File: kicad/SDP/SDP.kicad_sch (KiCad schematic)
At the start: 86 parts, among them J1 GPIO, J18 12V, J24 POWER, J25 Conn_01x04, J26 Conn_01x02, J27 MOTOR, J3 UART, J4 I2C, J5 Conn_01x04, J6 Conn_01x04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

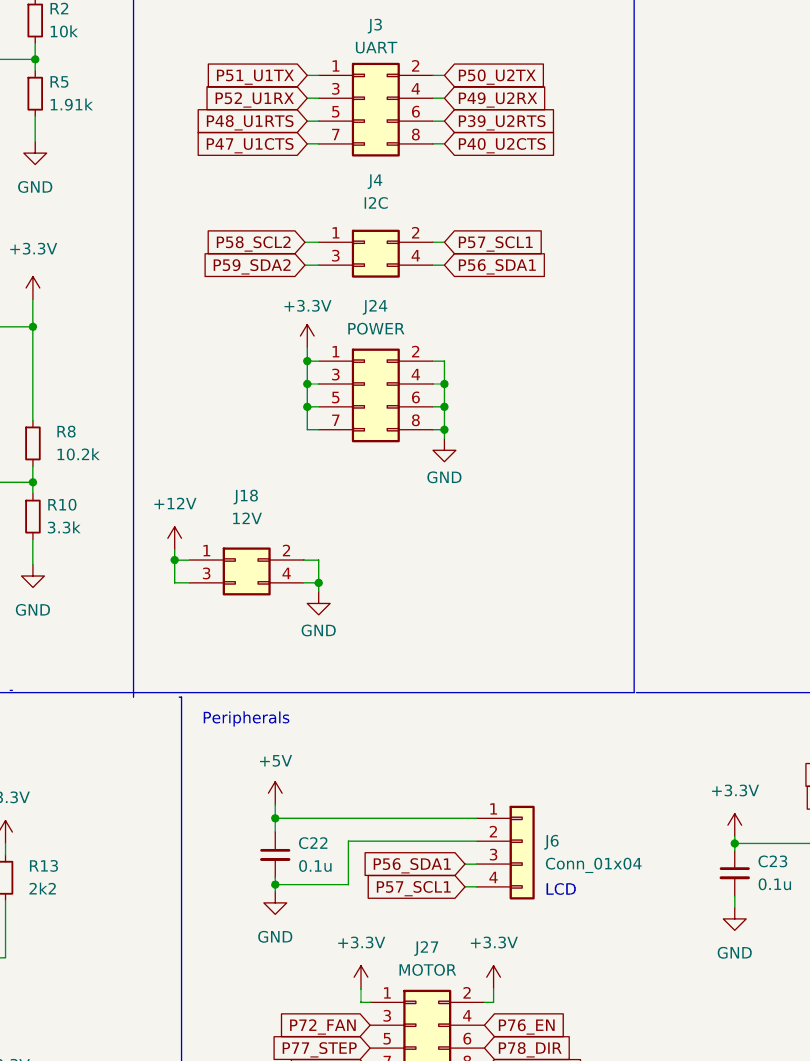
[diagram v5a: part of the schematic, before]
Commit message: Controller and motor PCB silkscreen and final layout
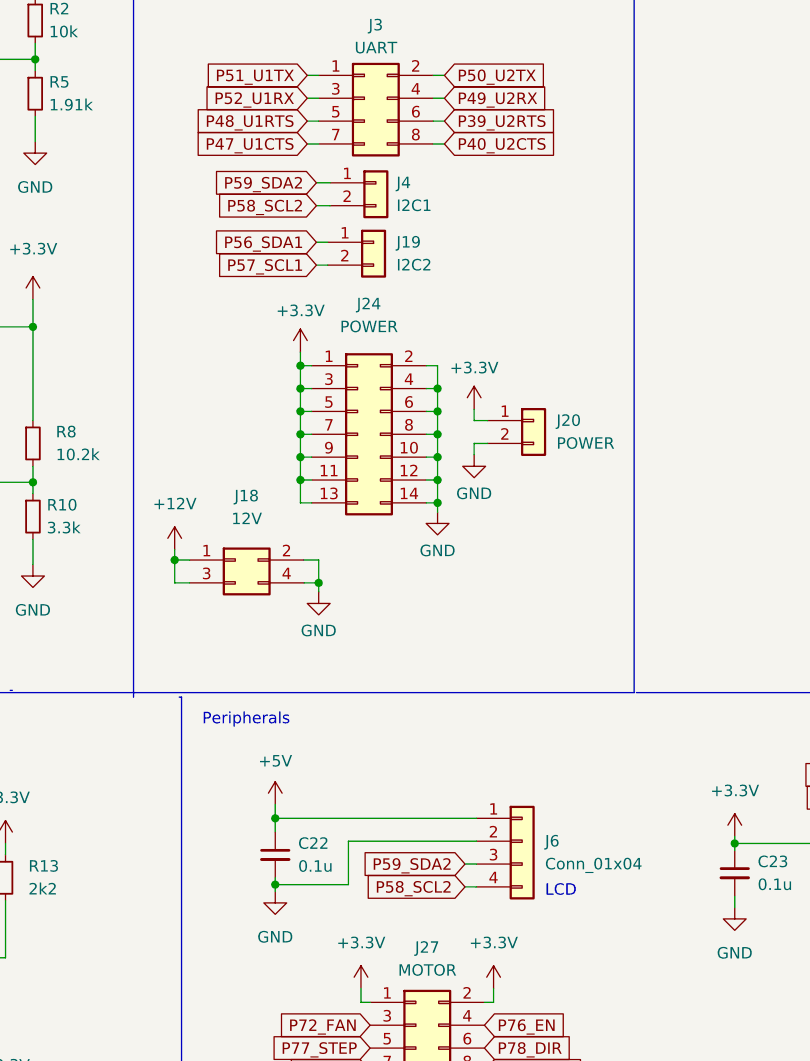
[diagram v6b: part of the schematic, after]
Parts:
- removed J24: POWER, Connector_PinSocket_2.54mm:PinSocket_2x04_P2.54mm_Vertical, symbol Connector_Generic:Conn_02x04_Odd_Even
- removed J4: I2C, Connector_PinSocket_2.54mm:PinSocket_2x02_P2.54mm_Vertical, symbol Connector_Generic:Conn_02x02_Odd_Even
- added J19: I2C2, Connector_PinSocket_2.54mm:PinSocket_1x02_P2.54mm_Vertical, symbol Connector_Generic:Conn_01x02
- added J20: POWER, Connector_PinSocket_2.54mm:PinSocket_1x02_P2.54mm_Vertical, symbol Connector_Generic:Conn_01x02
- added J24: POWER, Connector_PinSocket_2.54mm:PinSocket_2x07_P2.54mm_Vertical, symbol Connector_Generic:Conn_02x07_Odd_Even
- added J4: I2C1, Connector_PinSocket_2.54mm:PinSocket_1x02_P2.54mm_Vertical, symbol Connector_Generic:Conn_01x02
- Y2: footprint CFS206:CFS206-32.768-KDZF-UB -> Crystal:Crystal_DS26_D2.0mm_L6.0mm_Horizontal
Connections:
- net +3V3: now also J20.1 (Pin_1), J24.1 (Pin_1), J24.11 (Pin_11), J24.13 (Pin_13), J24.3 (Pin_3), J24.5 (Pin_5), J24.7 (Pin_7), J24.9 (Pin_9)
- net GND: now also J20.2 (Pin_2), J24.10 (Pin_10), J24.12 (Pin_12), J24.14 (Pin_14), J24.2 (Pin_2), J24.4 (Pin_4), J24.6 (Pin_6), J24.8 (Pin_8)
- net P56_SDA1: now also J19.1 (Pin_1); no longer J6.3 (Pin_3)
- net P57_SCL1: now also J19.2 (Pin_2); no longer J6.4 (Pin_4)
- net P58_SCL2: now also J6.4 (Pin_4), J4.2 (Pin_2)
- net P59_SDA2: now also J6.3 (Pin_3), J4.1 (Pin_1)

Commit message: Final PCB layout changes
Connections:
- net GND: no longer J27.15 (Pin_15)
- no-connect marks 12 -> 13
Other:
- moved on the sheet: J27
